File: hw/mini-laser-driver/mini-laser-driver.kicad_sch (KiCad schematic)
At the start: 27 parts, among them J1 Conn_01x05_Pin, Q1 MMBT3904, Q2 MMBT3906, Q3 BSS83P, U1 LMV358, U2 AD8605

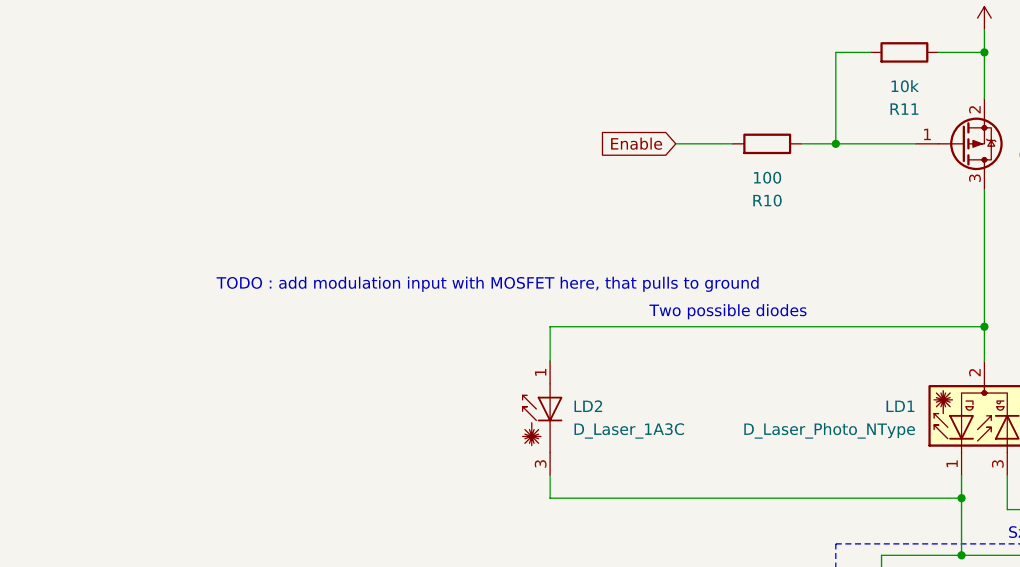
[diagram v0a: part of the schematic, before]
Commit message: Rename versions to concordate with what is written in schematic
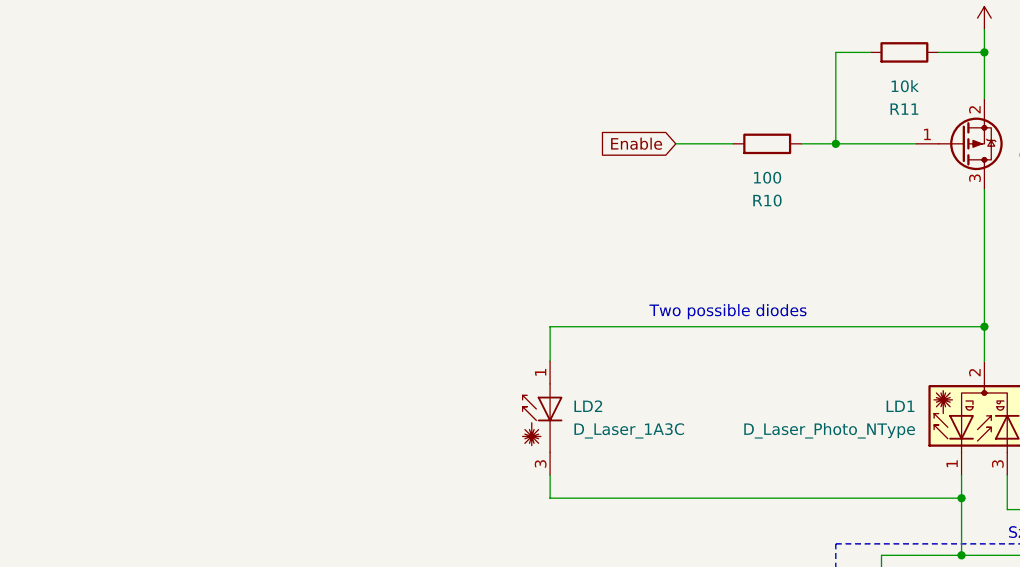
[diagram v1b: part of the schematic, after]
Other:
- note removed: "TODO : add modulation input with MOSFET here, that pulls to ground"
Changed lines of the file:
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@@
-		)
-	)
-	(text "TODO : add modulation input with MOSFET here, that pulls to ground"
-		(exclude_from_sim no)
-		(at 73.152 91.948 0)
-		(effects
-			(font
-				(size 1.27 1.27)
-			)
 		)
 	)
